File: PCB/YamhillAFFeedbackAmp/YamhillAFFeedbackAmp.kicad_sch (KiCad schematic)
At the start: 25 parts, among them J1 +12 VDC, J2 Output, J3 Input (50 Ω), Q1 2N4401, Q2 2N4401

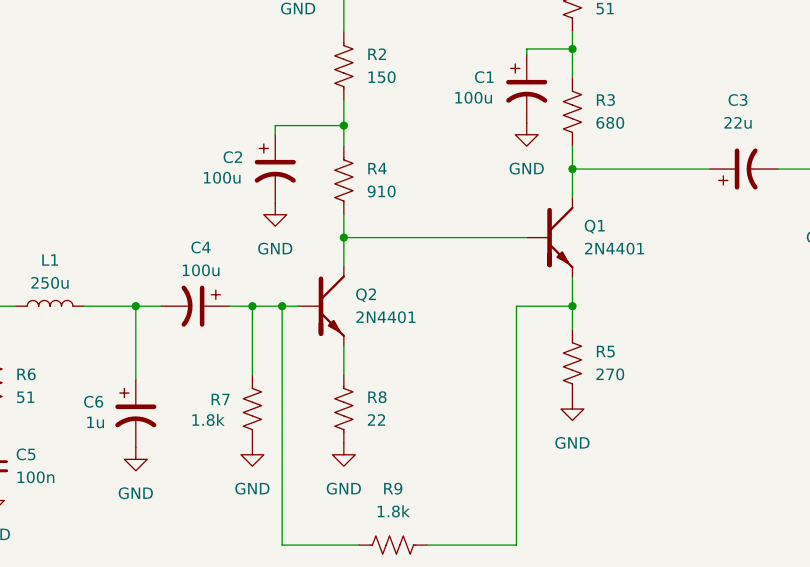
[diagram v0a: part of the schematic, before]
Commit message: Add Active AF Filter board
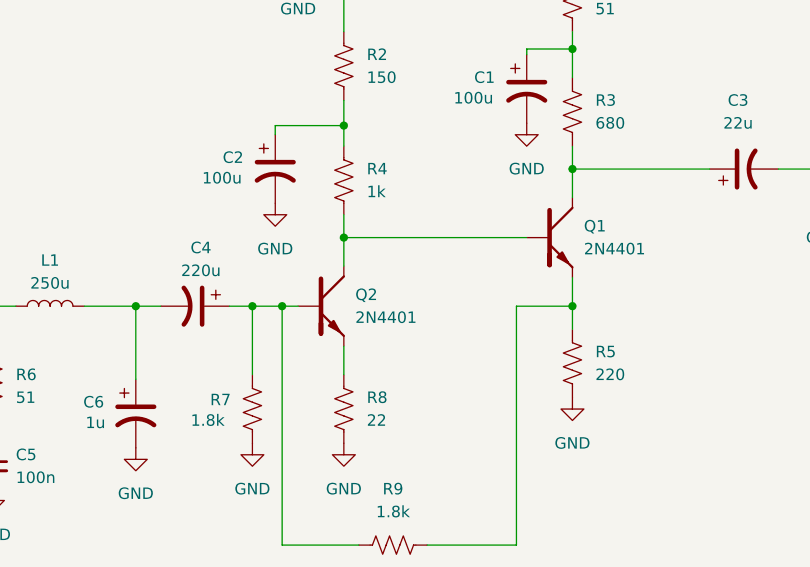
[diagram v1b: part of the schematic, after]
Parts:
- C4: value 100u -> 220u
- R4: value 910 -> 1k
- R5: value 270 -> 220
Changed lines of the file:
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@@
       (effects (font (size 1.27 1.27)) (justify left))
     )
-    (property "Value" "910" (at 136.906 89.027 0)
+    (property "Value" "1k" (at 136.906 89.027 0)
       (effects (font (size 1.27 1.27)) (justify left))
     )
@@
       (effects (font (size 1.27 1.27)))
     )
-    (property "Value" "100u" (at 118.491 97.79 90)
+    (property "Value" "220u" (at 118.491 97.79 90)
       (effects (font (size 1.27 1.27)))
     )
@@
       (effects (font (size 1.27 1.27)) (justify left))
     )
-    (property "Value" "270" (at 162.306 109.347 0)
-      (effects (font (size 1.27 1.27)) (justify left))
-    )
+    (property "Value" "220" (at 162.306 109.347 0)
+      (effects (font (size 1.27 1.27)) (justify left))
+    )
